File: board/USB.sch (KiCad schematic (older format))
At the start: 46 parts, among them J1 USB_MICRO_B, J7 USB_MICRO_B, P11 CONN_1, P12 CONN_1, P13 CONN_1, U18 USB3340, U2 CY7C68013A_100AC, X1 CRYSTAL

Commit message: Issue #1481 - DOC
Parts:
- added C? (x2): 0.1uFD, ~, symbol C
- added R?: 20R, ~, symbol R
- added U?: BDXXGA5WEFJ_, symbol BDXXGA5WEFJ_
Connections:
- net GND: now also C?.2, C?.2, U?.3 (GND), U?.9 (EP)
- net VBUS: now reaches C38.1, F2.1, R30.2
- net VBUS: now also R?.2
- net VCC5V0 renamed CPEN
- net CPEN: now also U?.5 (EN)
- new net: C?.1, R?.1, U?.1 (VO), U?.2 (FB/VOS)
- new net VCC12V0: C?.1, U?.8 (VCC)
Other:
- note removed: "?"
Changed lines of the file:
@@
 LIBS:contrib
 LIBS:valves
+LIBS:hdmi2usb
 LIBS:HDMI2USB-cache
+LIBS:Atlys-VHDCI-cache
 EELAYER 27 0
 EELAYER END
 $Descr A3 16535 11693
 encoding utf-8
-Sheet 11 11
+Sheet 10 12
 Title "HDMI2USB"
-Date "14 jan 2015"
-Rev ""
+Date "18 feb 2015"
+Rev "Rev2"
 Comp ""
 Comment1 ""
@@
 $EndComp
 $Comp
-L GND #PWR44
+L GND #PWR042
 U 1 1 54AFC1CB
 P 12750 9750
-F 0 "#PWR44" H 12750 9750 30  0001 C CNN
+F 0 "#PWR042" H 12750 9750 30  0001 C CNN
 F 1 "GND" H 12750 9680 30  0001 C CNN
 F 2 "" H 12750 9750 60  0000 C CNN
@@
 0D 08 60 00 00 34 20 80 01 00 D0 80 00 06 00 40 03 02 18 00 00 0D 08 60 00 00 34 20 80 01 00 D0
 80 00 06 00 40 03 02 18 00 00 0D FE 0D 6E A0 C3 78 63 AE 4C 0B 00 00 00 00 49 45 4E 44 AE 42 60
-82 01 $EndBitmap
+82 03 $EndBitmap
 EndData
 $EndBitmap
 $Comp
-L PWR_FLAG #FLG1
+L PWR_FLAG #FLG043
 U 1 1 54AFC1D5
 P 14850 3500
-F 0 "#FLG1" H 14850 3595 30  0001 C CNN
+F 0 "#FLG043" H 14850 3595 30  0001 C CNN
 F 1 "PWR_FLAG" H 14850 3680 30  0000 C CNN
 F 2 "" H 14850 3500 60  0000 C CNN
@@
 VCC3V3
 $Comp
-L GND #PWR43
+L GND #PWR044
 U 1 1 54AFC1E5
 P 10250 2500
-F 0 "#PWR43" H 10250 2500 30  0001 C CNN
+F 0 "#PWR044" H 10250 2500 30  0001 C CNN
 F 1 "GND" H 10250 2430 30  0001 C CNN
 F 2 "" H 10250 2500 60  0000 C CNN
@@
 	0    -1   -1   0
 $EndComp
-Text GLabel 5350 8900 2    60   Input ~ 0
-VCC5V0
 Text Notes 6450 8650 1    60   ~ 0
 5V@400mA
 Text Notes 2750 10450 0    60   ~ 0
 ID pin have three options can be connect this to \nVCC,GND,USB depending on the applications like \nDevice,Host,OTG
-Text Notes 5800 8900 0    60   ~ 0
-?
 $Comp
 L C C38
@@
 Text Label 6400 7850 0    60   ~ 0
 ID
-Text Label 5350 8900 2    60   ~ 0
-VCC5V0
 Text Label 5000 7100 2    60   ~ 0
 GND
@@
 Text Label 10500 5400 2    60   ~ 0
 GND
+$Comp
+L BDXXGA5WEFJ_ U?
+U 1 1 54E4C9BC
+P 10400 9150
+F 0 "U?" H 10100 8650 60  0000 C CNN
+F 1 "BDXXGA5WEFJ_" H 10350 9900 60  0000 C CNN
+F 2 "" H 10400 9150 60  0000 C CNN
+F 3 "" H 10400 9150 60  0000 C CNN
+	1    10400 9150
+	1    0    0    -1
+$EndComp
+Text GLabel 9100 8750 0    60   Input ~ 0
+VCC12V0
+Wire Wire Line
+	9100 8750 9850 8750
+Text Label 5350 8900 2    60   ~ 0
+CPEN
+Text Label 9350 8900 0    60   ~ 0
+CPEN
+Wire Wire Line
+	9350 8900 9850 8900
+Wire Wire Line
+	9850 9450 9850 9350
+Wire Wire Line
+	9150 9450 9850 9450
+Text Label 9350 9450 0    60   ~ 0
+GND
+Wire Wire Line
+	10850 8650 11300 8650
+Wire Wire Line
+	11050 8650 11050 9300
+Wire Wire Line
+	11050 9050 10850 9050
+Connection ~ 11050 8650
+Text Label 12000 8650 2    60   ~ 0
+VBUS
+Text Label 6350 8700 2    60   ~ 0
+VBUS
+$Comp
+L C C?
+U 1 1 54E4E68F
+P 11050 9500
+F 0 "C?" H 11050 9600 40  0000 L CNN
+F 1 "0.1uFD" H 11056 9415 40  0000 L CNN
+F 2 "~" H 11088 9350 30  0000 C CNN
+F 3 "~" H 11050 9500 60  0000 C CNN
+	1    11050 9500
+	1    0    0    -1
+$EndComp
+Text Label 11450 9700 2    60   ~ 0
+GND
+Wire Wire Line
+	11050 9700 11450 9700
+$Comp
+L C C?
+U 1 1 54E4EC64
+P 9150 9200
+F 0 "C?" H 9150 9300 40  0000 L CNN
+F 1 "0.1uFD" H 9156 9115 40  0000 L CNN
+F 2 "~" H 9188 9050 30  0000 C CNN
+F 3 "~" H 9150 9200 60  0000 C CNN
+	1    9150 9200
+	1    0    0    -1
+$EndComp
+Wire Wire Line
+	9150 8750 9150 9000
+Wire Wire Line
+	9150 9400 9150 9450
+Connection ~ 9150 8750
+$Comp
+L R R?
+U 1 1 54E500EF
+P 11550 8650
+F 0 "R?" V 11630 8650 40  0000 C CNN
+F 1 "20R" V 11557 8651 40  0000 C CNN
+F 2 "~" V 11480 8650 30  0000 C CNN
+F 3 "~" H 11550 8650 30  0000 C CNN
+	1    11550 8650
+	0    -1   -1   0
+$EndComp
+Wire Wire Line
+	11800 8650 12000 8650
+Connection ~ 11050 9050
 $EndSCHEMATC

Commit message: Issue #1473 - Fixing UTMI schematic and adding text descriptions.
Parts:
- removed C38: 0.1uFD, ~, symbol C
- removed F2: FUSE, ~, symbol FUSE
- removed R?: 20R, ~, symbol R
- R30: Power (none) -> 0.05W (min)
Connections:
- net VBUS is gone; now on net USB_5V: R30.2
- net USB_5V: now reaches J1.1 (+5V)
- net USB_5V: now also U?.1 (VO)
- net at C?.1, U?.2 (FB/VOS): no longer U?.1 (VO)
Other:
- note added: "Decoupling Capacitors"
- note added: "USB 2.0 Device Port\nJTAG Programmer and "Easy" High Speed USB 2.0 Interface\nCypress FX2 based"
- note added: "USB 2.0 OTG Port (Host + Device Support)\nUTMI+/ULPI IC - Require full FPGA USB2.0 stack\nMicrochip USB3440\nFOSS Cores:\n * Daisho - http://goo.gl/eSwTeb\n * joris_vr - http://jorisvr.nl/usb/\n"
- note added: "Which ICs are these for!?"
- note removed: "5V@400mA"
- note removed: "ID pin have three options can be connect this to \nVCC,GND,USB depending on the applications like \nDevice,Host,OTG"
- moved on the sheet: C34, C35, C37, C?, J1, R13, R30, U18, U2A, U2B, U2C, U?

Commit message: Issue #1481 - GPIO sheet
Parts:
- R30: value 20K -> 20K5%- 0.05W
- gave numbers to parts that had none: 3
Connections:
- net USB_5V: now also C240.1, U24.2 (FB/VOS)
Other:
- note added: "Cypress CY7C68013A\nDecoupling Capacitors"
- note removed: "Decoupling Capacitors"
- note removed: "Which ICs are these for!?"
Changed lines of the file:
@@
 LIBS:valves
 LIBS:hdmi2usb
+LIBS:timvideos-pcie-8x
 LIBS:HDMI2USB-cache
-LIBS:Atlys-VHDCI-cache
-EELAYER 25 0
+EELAYER 27 0
 EELAYER END
 $Descr A3 16535 11693
@@
 Sheet 10 12
 Title "HDMI2USB"
-Date "18 feb 2015"
+Date "20 feb 2015"
 Rev "Rev2"
 Comp ""
@@
 $EndComp
 $Comp
-L GND #PWR042
+L GND #PWR40
 U 1 1 54AFC1CB
 P 12750 9750
-F 0 "#PWR042" H 12750 9750 30  0001 C CNN
+F 0 "#PWR40" H 12750 9750 30  0001 C CNN
 F 1 "GND" H 12750 9680 30  0001 C CNN
 F 2 "" H 12750 9750 60  0000 C CNN
@@
 0D 08 60 00 00 34 20 80 01 00 D0 80 00 06 00 40 03 02 18 00 00 0D 08 60 00 00 34 20 80 01 00 D0
 80 00 06 00 40 03 02 18 00 00 0D FE 0D 6E A0 C3 78 63 AE 4C 0B 00 00 00 00 49 45 4E 44 AE 42 60
-82 FF
+82 04 $EndBitmap
 EndData
 $EndBitmap
 $Comp
-L PWR_FLAG #FLG043
+L PWR_FLAG #FLG1
 U 1 1 54AFC1D5
 P 14850 3500
-F 0 "#FLG043" H 14850 3595 30  0001 C CNN
+F 0 "#FLG1" H 14850 3595 30  0001 C CNN
 F 1 "PWR_FLAG" H 14850 3680 30  0000 C CNN
 F 2 "" H 14850 3500 60  0000 C CNN
@@
 VCC3V3
 $Comp
-L GND #PWR044
+L GND #PWR39
 U 1 1 54AFC1E5
 P 10250 2500
-F 0 "#PWR044" H 10250 2500 30  0001 C CNN
+F 0 "#PWR39" H 10250 2500 30  0001 C CNN
 F 1 "GND" H 10250 2430 30  0001 C CNN
 F 2 "" H 10250 2500 60  0000 C CNN
@@
 P 3750 9000
 F 0 "R30" V 3830 9000 40  0000 C CNN
-F 1 "20K" V 3757 9001 40  0000 C CNN
+F 1 "20K5%- 0.05W" V 3650 9000 40  0000 C CNN
 F 2 "~" V 3680 9000 30  0000 C CNN
 F 3 "~" H 3750 9000 30  0000 C CNN
@@
 GND
 $Comp
-L BDXXGA5WEFJ_ U?
+L BDXXGA5WEFJ_ U24
 U 1 1 54E4C9BC
 P 4850 10050
-F 0 "U?" H 4550 9550 60  0000 C CNN
+F 0 "U24" H 4550 9550 60  0000 C CNN
 F 1 "BDXXGA5WEFJ_" H 4800 10800 60  0000 C CNN
 F 2 "" H 4850 10050 60  0000 C CNN
@@
 GND
 $Comp
-L C C?
+L C C240
 U 1 1 54E4E68F
 P 5700 10150
-F 0 "C?" H 5700 10250 40  0000 L CNN
+F 0 "C240" H 5700 10250 40  0000 L CNN
 F 1 "0.1uFD" H 5706 10065 40  0000 L CNN
 F 2 "~" H 5738 10000 30  0000 C CNN
@@
 $EndComp
 $Comp
-L C C?
+L C C38
 U 1 1 54E4EC64
 P 4150 10050
-F 0 "C?" H 4150 10150 40  0000 L CNN
+F 0 "C38" H 4150 10150 40  0000 L CNN
 F 1 "0.1uFD" H 4156 9965 40  0000 L CNN
 F 2 "~" H 4188 9900 30  0000 C CNN
@@
 USB_5V
 $Comp
-L GND #PWR?
+L GND #PWR38
 U 1 1 54E5E8EF
 P 2500 11000
-F 0 "#PWR?" H 2500 11000 30  0001 C CNN
+F 0 "#PWR38" H 2500 11000 30  0001 C CNN
 F 1 "GND" H 2500 10930 30  0001 C CNN
 F 2 "" H 2500 11000 60  0000 C CNN
@@
 	1    0    0    -1
 $EndComp
-Text Notes 650  7100 0    157  ~ 0
+Text Notes 700  6000 0    118  ~ 24
 USB 2.0 OTG Port (Host + Device Support)\nUTMI+/ULPI IC - Require full FPGA USB2.0 stack\nMicrochip USB3440\nFOSS Cores:\n * Daisho - http://goo.gl/eSwTeb\n * joris_vr - http://jorisvr.nl/usb/\n
-Text Notes 650  1250 0    157  ~ 0
+Text Notes 650  850  0    118  ~ 24
 USB 2.0 Device Port\nJTAG Programmer and "Easy" High Speed USB 2.0 Interface\nCypress FX2 based
 Wire Wire Line
@@
 	4150 10350 4300 10350
 Wire Wire Line
-	5500 9000 5500 9900
+	5500 9000 5500 9950
 Wire Wire Line
 	5300 9950 5700 9950
@@
 Wire Notes Line
 	10550 5600 10550 11200
-Text Notes 11750 8400 0    197  ~ 0
-Decoupling Capacitors
-Text Notes 11850 8800 0    157  Italic 0
-Which ICs are these for!?
+Text Notes 12150 8850 0    118  ~ 24
+Cypress CY7C68013A\nDecoupling Capacitors
 $EndSCHEMATC

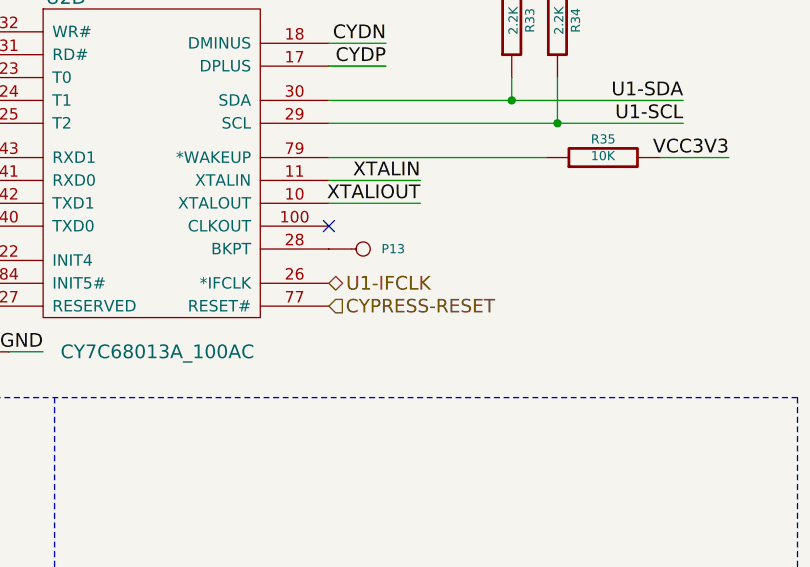
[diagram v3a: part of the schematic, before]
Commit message: Issue #1481 - CYPRESS-FPGA CONNECTIONS ADDED
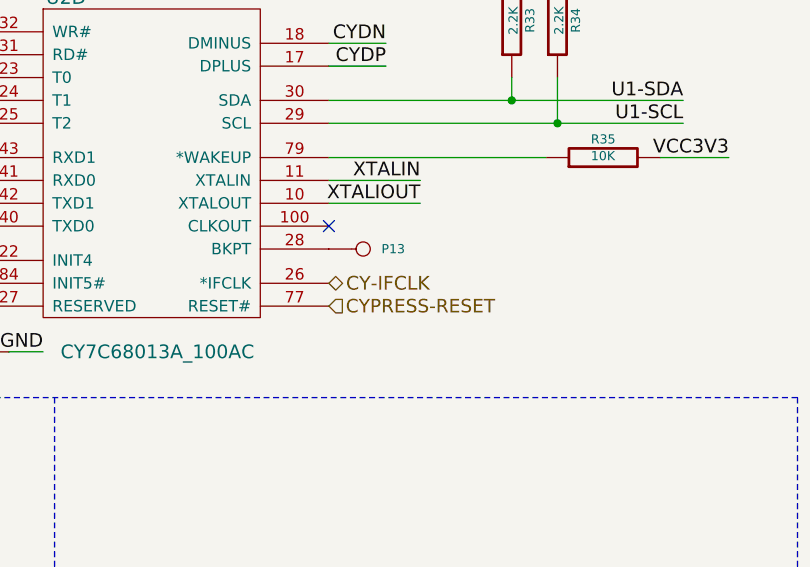
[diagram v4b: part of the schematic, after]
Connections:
- net U1-IFCLK renamed CY-IFCLK
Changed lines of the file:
@@
 $Descr A3 16535 11693
 encoding utf-8
-Sheet 10 12
+Sheet 9 12
 Title "HDMI2USB"
-Date "20 feb 2015"
+Date "24 feb 2015"
 Rev "Rev2"
 Comp ""
@@
 $EndComp
 $Comp
-L GND #PWR40
+L GND #PWR038
 U 1 1 54AFC1CB
 P 12750 9750
-F 0 "#PWR40" H 12750 9750 30  0001 C CNN
+F 0 "#PWR038" H 12750 9750 30  0001 C CNN
 F 1 "GND" H 12750 9680 30  0001 C CNN
 F 2 "" H 12750 9750 60  0000 C CNN
@@
 GND
 Text HLabel 11750 5100 2    60   BiDi ~ 0
-U1-IFCLK
+CY-IFCLK
 NoConn ~ 15100 4050
 $Comp
@@
 0D 08 60 00 00 34 20 80 01 00 D0 80 00 06 00 40 03 02 18 00 00 0D 08 60 00 00 34 20 80 01 00 D0
 80 00 06 00 40 03 02 18 00 00 0D FE 0D 6E A0 C3 78 63 AE 4C 0B 00 00 00 00 49 45 4E 44 AE 42 60
-82 04 $EndBitmap
+82 01 $EndBitmap
 EndData
 $EndBitmap
 $Comp
-L PWR_FLAG #FLG1
+L PWR_FLAG #FLG039
 U 1 1 54AFC1D5
 P 14850 3500
-F 0 "#FLG1" H 14850 3595 30  0001 C CNN
+F 0 "#FLG039" H 14850 3595 30  0001 C CNN
 F 1 "PWR_FLAG" H 14850 3680 30  0000 C CNN
 F 2 "" H 14850 3500 60  0000 C CNN
@@
 VCC3V3
 $Comp
-L GND #PWR39
+L GND #PWR040
 U 1 1 54AFC1E5
 P 10250 2500
-F 0 "#PWR39" H 10250 2500 30  0001 C CNN
+F 0 "#PWR040" H 10250 2500 30  0001 C CNN
 F 1 "GND" H 10250 2430 30  0001 C CNN
 F 2 "" H 10250 2500 60  0000 C CNN
@@
 USB_5V
 $Comp
-L GND #PWR38
+L GND #PWR041
 U 1 1 54E5E8EF
 P 2500 11000
-F 0 "#PWR38" H 2500 11000 30  0001 C CNN
+F 0 "#PWR041" H 2500 11000 30  0001 C CNN
 F 1 "GND" H 2500 10930 30  0001 C CNN
 F 2 "" H 2500 11000 60  0000 C CNN
